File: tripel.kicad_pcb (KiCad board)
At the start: 2 copper layers, 95.1 x 97.4 mm, 58 parts, among them J1 Left Columns, J4 Right Columns, J6 USB_mini_micro_B, K1.1 KEYSW, K1.2 KEYSW, K1.3 KEYSW, K1.4 KEYSW, K1.5 KEYSW, K2.1 KEYSW, K2.2 KEYSW, K2.3 KEYSW, K2.4 KEYSW, K2.5 KEYSW, K3.1 KEYSW, K3.2 KEYSW, K3.3 KEYSW, K3.4 KEYSW, K3.5 KEYSW, K4.1 KEYSW, K4.2 KEYSW, K4.3 KEYSW, K4.4 KEYSW, K4.5 KEYSW, K5.1 KEYSW, K5.2 KEYSW, K5.3 KEYSW, K5.4 KEYSW, U1 ProMicro_ChipSideDown

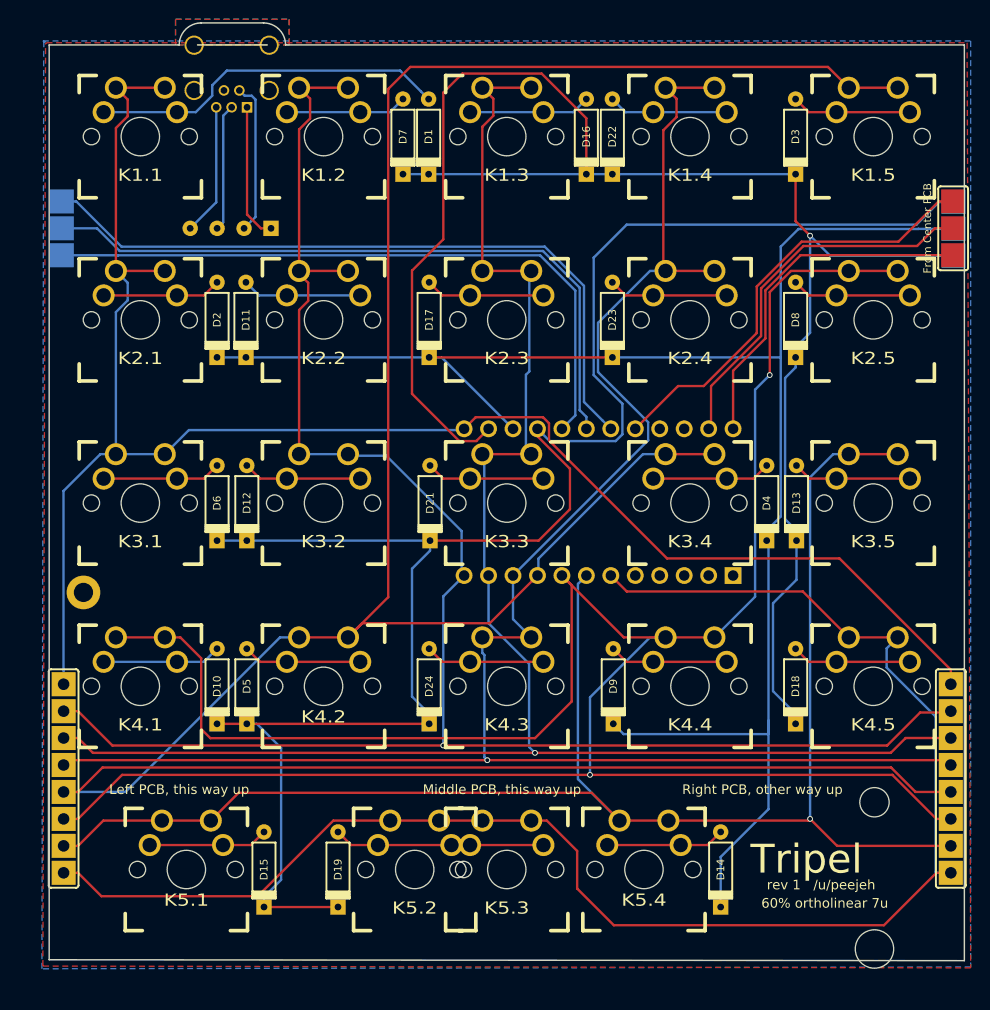
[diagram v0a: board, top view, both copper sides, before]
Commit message: Add split spacebar bottom row
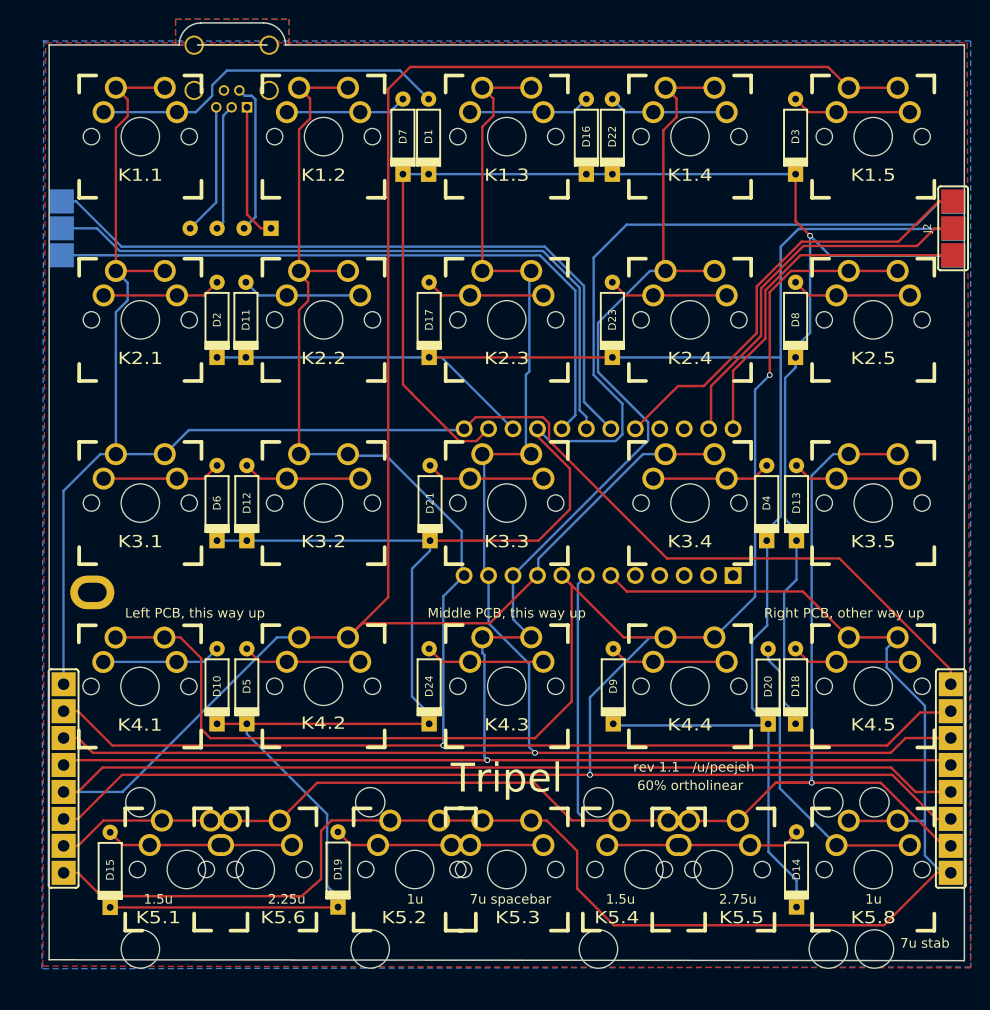
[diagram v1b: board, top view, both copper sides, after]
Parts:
- added D20: D, keyboard:DIODE, F.Cu at (186.5, 104.7)
- added K5.5: KEYSW, keyboard:MX_DBL_275, F.Cu at (180.8, 123.8)
- added K5.6: KEYSW, keyboard:MX_DBL_225, F.Cu at (133.3, 123.7)
- added K5.8: KEYSW, keyboard:MX_DOUBLESIDED, F.Cu at (197.4, 123.8)
- J2: renamed from From Center PCB
- J3: renamed from To Left PCB
- J5: renamed from To Right PCB
- moved D15 16.0 mm to (118.2, 123.8)
- moved D14 7.88 mm to (189.5, 123.8)
- moved REF** 0.92 mm to (116.3, 95.0)
- renumbered USB to J7
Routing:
- net Net-(D1-Pad1): track 184.4 -> 150.6 mm
- net Net-(D20-Pad2): track 0.00 -> 31.0 mm
- net Net-(D10-Pad1): track 188.9 -> 206.0 mm
- net Net-(J1-Pad1): track 166.5 -> 176.9 mm
- net Net-(D14-Pad2): track 12.3 -> 20.4 mm
- net Net-(D15-Pad2): track 12.4 -> 19.4 mm
- net Net-(J1-Pad2): track 170.1 -> 176.9 mm
- net Net-(D11-Pad1): track 178.3 -> 177.6 mm
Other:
- board text added: "1.5u"
- board text added: "1u"
- board text added: "2.25u"
- board text added: "2.75u"
- board text added: "60% ortholinear"
- board text added: "7u spacebar"
- board text added: "7u stab"
- board text added: "Middle PCB only"
- board text added: "rev 1.1 /u/peejeh"
- board text removed: "60% ortholinear 7u"
- board text removed: "rev 1 /u/peejeh"

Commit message: Increase size of mounting hole to ease case installation
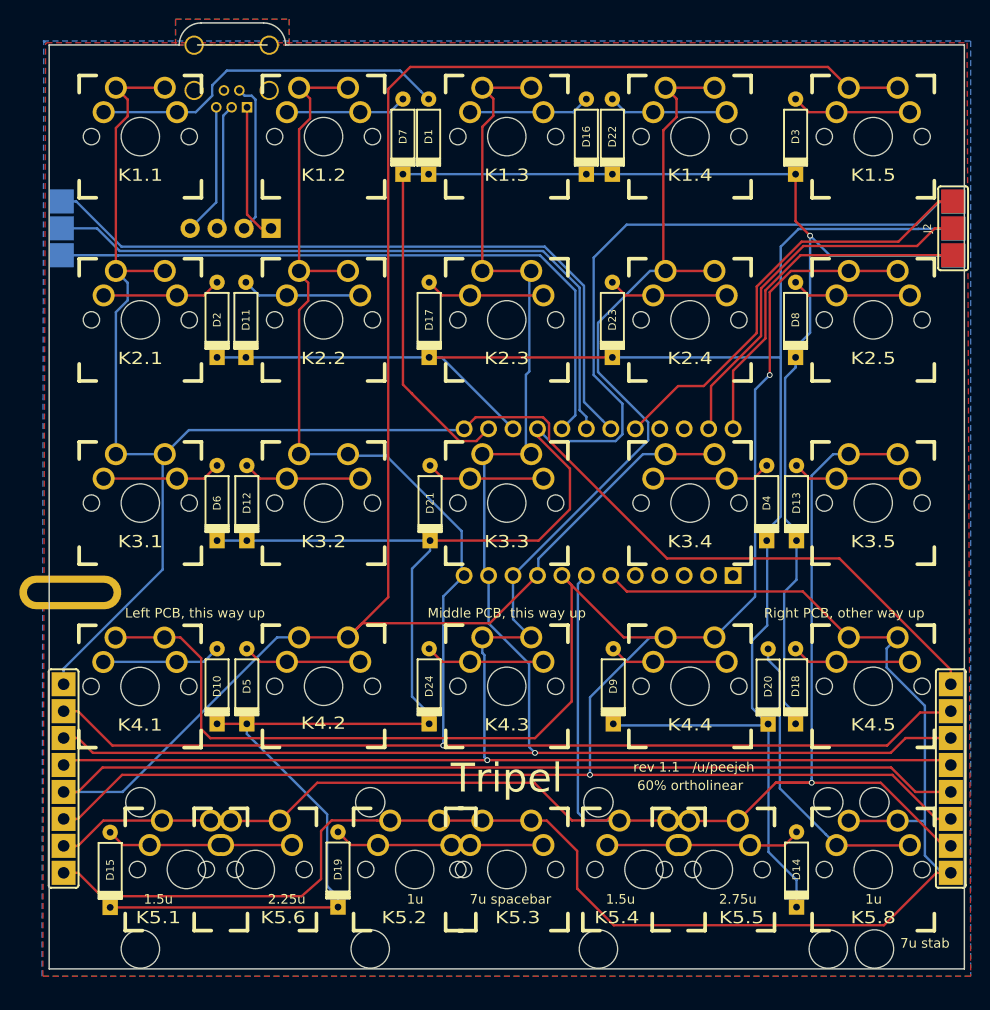
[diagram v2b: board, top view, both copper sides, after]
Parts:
- moved REF** 2.29 mm to (114.0, 95.0)
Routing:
- net Net-(J1-Pad8): track 179.1 -> 180.3 mm
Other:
- board size 95.1 x 97.4 mm -> 95.1 x 98.3 mm
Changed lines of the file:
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@@
     (thickness 1.6)
     (drawings 262)
-    (tracks 450)
+    (tracks 451)
     (zones 0)
     (modules 62)
@@
     (40 Dwgs.User user hide)
     (41 Cmts.User user hide)
-    (42 Eco1.User user)
+    (42 Eco1.User user hide)
     (43 Eco2.User user hide)
     (44 Edge.Cuts user)
@@
     (mod_text_size 1 1)
     (mod_text_width 0.15)
-    (pad_size 1.6 1.6)
-    (pad_drill 0.7)
+    (pad_size 2 2)
+    (pad_drill 1.0922)
     (pad_to_mask_clearance 0.2)
     (aux_axis_origin 0 0)
@@
     (add_net "Net-(U1-Pad5)")
   )
-  (module footprints:Mounting_M2 locked (layer F.Cu)
-    (at 116.322 94.96875)
+  (module footprints:Mounting_M2 (layer F.Cu)
+    (at 114.036 94.96875)
     (fp_text reference REF** (at 0 -3.81) (layer F.SilkS) hide
       (effects (font (size 1 1) (thickness 0.15)))
@@
       (effects (font (size 1 1) (thickness 0.15)))
     )
-    (pad 1 thru_hole oval (at 0 0) (size 4.6 3.5) (drill oval 3 2) (layers *.Cu *.Mask F.SilkS))
+    (pad 1 thru_hole oval (at 0 0) (size 10.6 3.5) (drill oval 9 2) (layers *.Cu *.Mask F.SilkS))
   )
   (module keyboard:MX_DBL_275 (layer F.Cu)
@@
     (fp_arc (start -5.506 -1.3) (end -5.506 -1.55) (angle -90) (layer B.SilkS) (width 0.2))
     (fp_arc (start -5.506 1.3) (end -5.756 1.3) (angle -90) (layer B.SilkS) (width 0.2))
-    (pad 4 thru_hole circle (at 4.194 0 180) (size 1.6 1.6) (drill 0.7) (layers *.Cu *.Mask)
+    (pad 4 thru_hole circle (at 4.194 0 180) (size 2 2) (drill 1.0922) (layers *.Cu *.Mask)
       (net 52 "Net-(J6-Pad5)") (clearance 0.1))
-    (pad 2 thru_hole circle (at -1.406 0 180) (size 1.6 1.6) (drill 0.7) (layers *.Cu *.Mask)
+    (pad 2 thru_hole circle (at -1.406 0 180) (size 2 2) (drill 1.0922) (layers *.Cu *.Mask)
       (net 49 "Net-(J6-Pad2)") (clearance 0.1))
-    (pad 3 thru_hole circle (at 1.394 0 180) (size 1.6 1.6) (drill 0.7) (layers *.Cu *.Mask)
+    (pad 3 thru_hole circle (at 1.394 0 180) (size 2 2) (drill 1.0922) (layers *.Cu *.Mask)
       (net 50 "Net-(J6-Pad3)") (clearance 0.1))
-    (pad 1 thru_hole rect (at -4.206 0 180) (size 1.6 1.6) (drill 0.7) (layers *.Cu *.Mask)
+    (pad 1 thru_hole rect (at -4.206 0 180) (size 2 2) (drill 1.0922) (layers *.Cu *.Mask)
       (net 48 "Net-(J6-Pad1)") (clearance 0.1))
   )
@@
     (effects (font (size 3 3) (thickness 0.45)))
   )
-  (gr_line (start 111.84375 133.125) (end 111.84375 38.1) (layer Edge.Cuts) (width 0.15))
-  (gr_line (start 206.90625 133.21875) (end 111.84375 133.125) (layer Edge.Cuts) (width 0.15))
-  (gr_line (start 206.90625 38.1) (end 206.90625 133.21875) (layer Edge.Cuts) (width 0.15))
+  (gr_line (start 111.84375 134.0745) (end 111.84375 38.1) (layer Edge.Cuts) (width 0.15))
+  (gr_line (start 206.90625 134.0745) (end 111.84375 134.0745) (layer Edge.Cuts) (width 0.15))
+  (gr_line (start 206.90625 38.1) (end 206.90625 134.0745) (layer Edge.Cuts) (width 0.15))
   (gr_line (start 114.332148 54.638388) (end 114.332148 40.638788) (layer Eco1.User) (width 0.1))
   (gr_line (start 128.332988 54.638388) (end 114.332148 54.638388) (layer Eco1.User) (width 0.1))
@@
   (segment (start 120 64.629084) (end 118.7725 65.856584) (width 0.25) (layer B.Cu) (net 40))
   (segment (start 120 62.80375) (end 120 64.629084) (width 0.25) (layer B.Cu) (net 40))
-  (segment (start 117.156054 80.6075) (end 118.7725 80.6075) (width 0.25) (layer B.Cu) (net 40) (status 20))
   (segment (start 113.34375 103.006) (end 113.331249 102.993499) (width 0.25) (layer B.Cu) (net 40))
-  (segment (start 113.331249 84.432305) (end 117.156054 80.6075) (width 0.25) (layer B.Cu) (net 40))
-  (segment (start 113.331249 102.993499) (end 113.331249 84.432305) (width 0.25) (layer B.Cu) (net 40))
-  (segment (start 113.34375 104.506) (end 113.34375 103.006) (width 0.25) (layer B.Cu) (net 40) (status 10))
   (segment (start 205.5 103.006) (end 205.5 104.506) (width 0.25) (layer F.Cu) (net 40) (status 20))
   (segment (start 193.934 91.44) (end 205.5 103.006) (width 0.25) (layer F.Cu) (net 40))
@@
   (segment (start 154.81225 78.105) (end 126.355 78.105) (width 0.25) (layer B.Cu) (net 40) (status 10))
   (segment (start 154.9435 77.97375) (end 154.81225 78.105) (width 0.25) (layer B.Cu) (net 40) (status 30))
+  (segment (start 113.34375 102.876108) (end 113.34375 103.006) (width 0.25) (layer B.Cu) (net 40))
+  (segment (start 113.34375 103.006) (end 113.34375 104.506) (width 0.25) (layer B.Cu) (net 40))
+  (segment (start 123.631401 92.588457) (end 113.34375 102.876108) (width 0.25) (layer B.Cu) (net 40))
+  (segment (start 123.631401 80.828599) (end 123.631401 92.588457) (width 0.25) (layer B.Cu) (net 40))
+  (segment (start 123.8525 80.6075) (end 123.631401 80.828599) (width 0.25) (layer B.Cu) (net 40))
   (segment (start 180.594 77.72325) (end 180.3435 77.97375) (width 0.25) (layer F.Cu) (net 41) (status 30))
   (segment (start 180.594 73.533) (end 180.594 77.72325) (width 0.25) (layer F.Cu) (net 41) (status 20))
@@
     (polygon
       (pts
-        (xy 111.1875 37.6875) (xy 207.5625 37.6875) (xy 207.5625 133.875) (xy 111.09375 134.0625) (xy 111.28125 37.78125)
+        (xy 111.1875 37.6875) (xy 207.5625 37.6875) (xy 207.5625 134.8365) (xy 111.09375 134.8365) (xy 111.28125 37.78125)
         (xy 111.46875 37.78125)
       )
@@
     (polygon
       (pts
-        (xy 111.5625 37.875) (xy 207.1875 37.875) (xy 207.5625 133.96875) (xy 111.1875 133.78125) (xy 111.46875 37.96875)
+        (xy 111.5625 37.875) (xy 207.1875 37.875) (xy 207.5625 134.8365) (xy 111.1875 134.8365) (xy 111.46875 37.96875)
       )
     )

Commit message: Flip stabilizer mounting holes
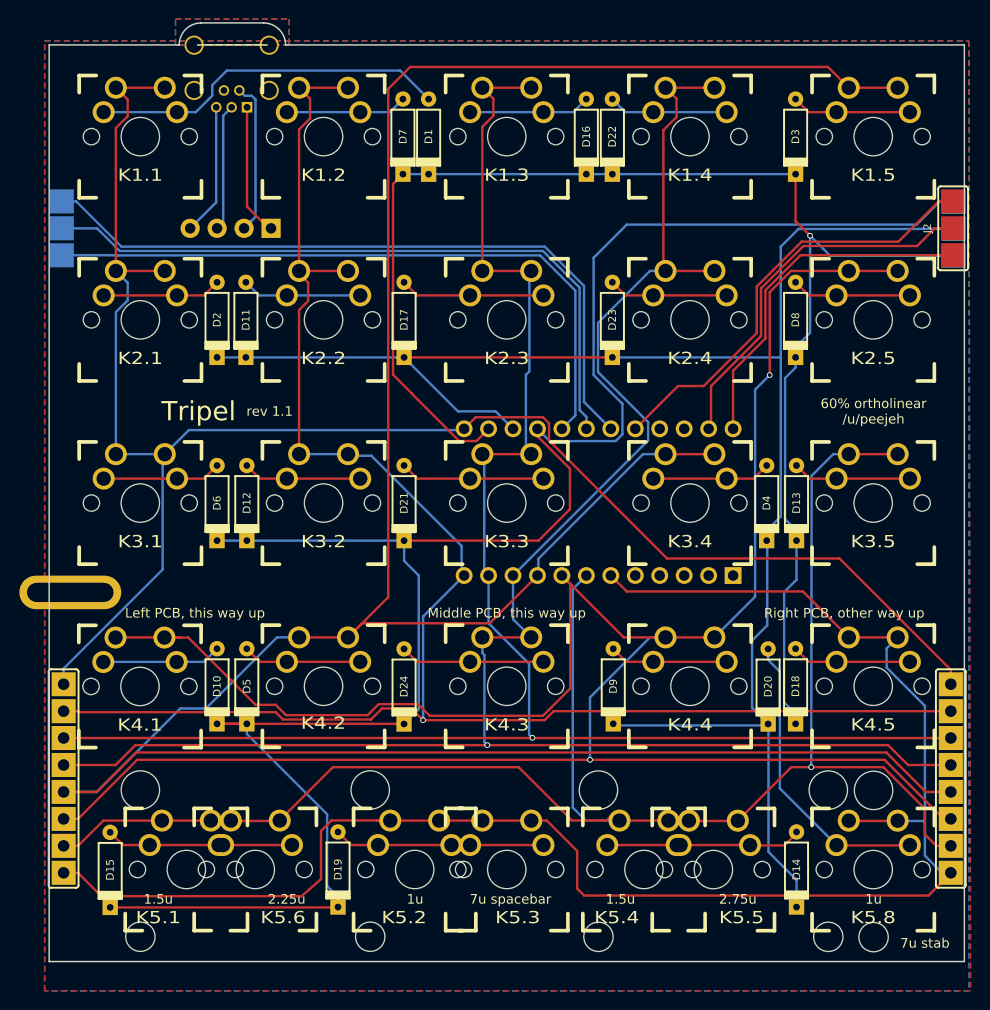
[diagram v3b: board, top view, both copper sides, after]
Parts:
- moved REF** 16.5 mm to (197.5, 115.5)
- moved REF** 14.0 mm to (197.5, 130.8)
- moved D21 2.70 mm to (148.7, 85.7)
- moved D24 2.61 mm to (148.7, 104.7)
- moved D17 2.61 mm to (148.7, 66.7)
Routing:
- net Net-(J1-Pad7): track 188.5 -> 184.8 mm
- net Net-(J1-Pad3): track 256.4 -> 253.0 mm
- net Net-(J1-Pad6): track 182.3 -> 179.4 mm
- net Net-(D21-Pad2): track 12.3 -> 15.0 mm
- net Net-(D17-Pad2): track 12.4 -> 15.0 mm
- net Net-(D11-Pad1): track 177.6 -> 180.2 mm
- net Net-(D24-Pad2): track 12.4 -> 15.0 mm
- net Net-(J1-Pad1): track 176.9 -> 174.4 mm
- net Net-(J1-Pad4): track 290.8 -> 292.1 mm
- net Net-(D10-Pad1): track 206.0 -> 206.9 mm
- net Net-(D1-Pad1): track 150.6 -> 151.4 mm
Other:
- board size 95.1 x 98.3 mm -> 95.1 x 97.5 mm
- board text added: "60% ortholinear /u/peejeh"
- board text added: "rev 1.1"
- board text removed: "60% ortholinear"
- board text removed: "rev 1.1 /u/peejeh"

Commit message: Fix right side PCB connection
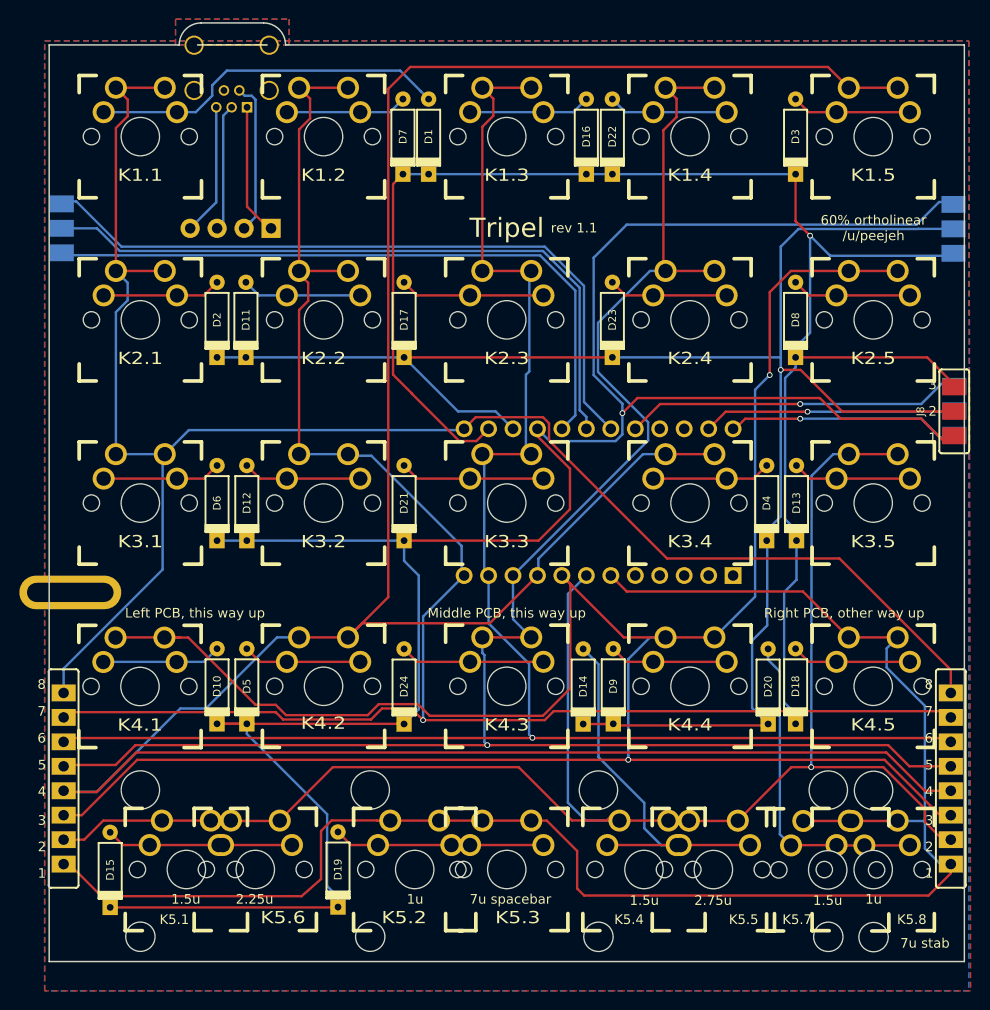
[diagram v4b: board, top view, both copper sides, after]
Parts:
- added J8: Right Rows, keyboard:CONNECTOR_3, F.Cu at (205.9, 76.2)
- added K5.7: KEYSW, keyboard:MX_DBL_150, F.Cu at (192.7, 123.8)
- D1, D10, D11, D12, D13, D14, D15, D16, D17, D18, D19, D2, D21, D22, D23, D24, D3, D4, D5, D6, D7, D8, D9: footprint footprints:DIODE -> keyboard:DIODE
- J1, J4: footprint footprints:CONNECTOR_8 -> keyboard:CONNECTOR_8
- J2: footprint footprints:CONNECTOR_3 -> keyboard:CONNECTOR_3; moved to B.Cu
- J3: footprint footprints:CONNECTOR_3 -> keyboard:CONNECTOR_3
- J5: value Rows -> Left Rows; footprint footprints:CONNECTOR_3 -> keyboard:CONNECTOR_3
- K1.1, K1.2, K1.3, K1.4, K1.5, K2.1, K2.2, K2.3, K2.4, K2.5, K3.1, K3.2, K3.3, K3.4, K3.5, K4.1, K4.2, K4.3, K4.4, K4.5, K5.2, K5.3: footprint footprints:MX_DOUBLESIDED -> keyboard:MX_DOUBLESIDED
- K5.1, K5.4: footprint footprints:MX_DOUBLESIDED -> keyboard:MX_DBL_150
- U1: footprint footprints:Pro_Micro_ChipSideDown -> keyboard:Pro_Micro_ChipSideDown
- moved D14 29.2 mm to (167.3, 104.7)
- moved J2 18.9 mm to (205.9, 76.1)
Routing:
- net Net-(D10-Pad1): track 206.9 -> 244.0 mm, vias 0 -> 1
- net Net-(D14-Pad2): track 20.4 -> 40.2 mm
- net Net-(D1-Pad1): track 151.4 -> 169.1 mm
- net Net-(J2-Pad2): track 39.4 -> 26.3 mm, vias 0 -> 1
- net Net-(J2-Pad3): track 36.8 -> 24.2 mm, vias 0 -> 1
- net Net-(J2-Pad1): track 45.6 -> 35.1 mm, vias 0 -> 1
- net Net-(J1-Pad1): track 174.4 -> 181.8 mm
- net Net-(D20-Pad2): track 31.0 -> 33.8 mm
- net Net-(D11-Pad1): track 180.2 -> 182.4 mm, vias 0 -> 1
- net Net-(J1-Pad8): track 180.3 -> 182.1 mm
- net Net-(J1-Pad2): track 176.9 -> 175.3 mm
- net Net-(J1-Pad3): track 253.0 -> 251.6 mm
- net Net-(J1-Pad7): track 184.8 -> 185.6 mm
